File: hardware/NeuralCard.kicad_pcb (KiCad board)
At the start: 2 copper layers, 85.6 x 54 mm, 57 parts, among them J1 ProgPads, SW1 SW-SMD_4P-L5.1-W5.1-P3.70-LS6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, SW2 SW-SMD_4P-L5.1-W5.1-P3.70-LS6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, SW3 SW_SPDT_Shouhan_MSK12C02, U1 WIRELM-SMD_ESP32-S3-WROOM-1, U2 LGA-14_L3.0-W2.5-P0.50-TL, U4 SO-8_L4.9-W3.9-P1.27-LS5.9-BL

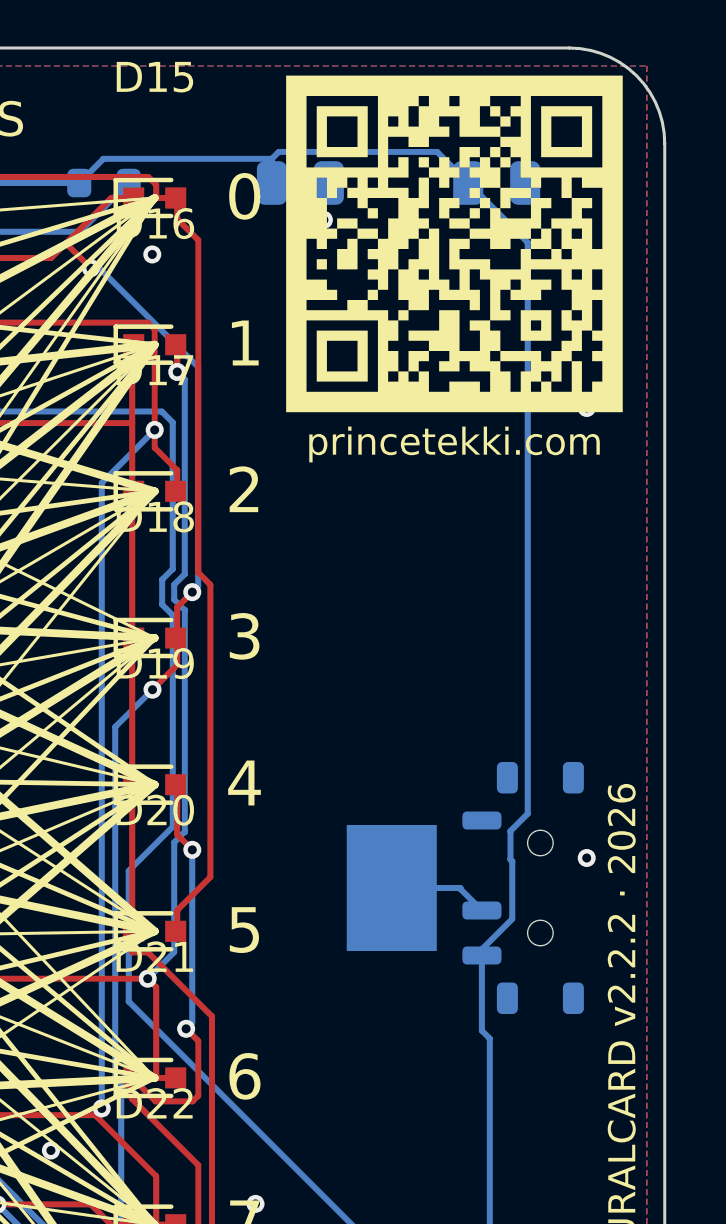
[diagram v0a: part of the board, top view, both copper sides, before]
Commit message: feat: place usb parts
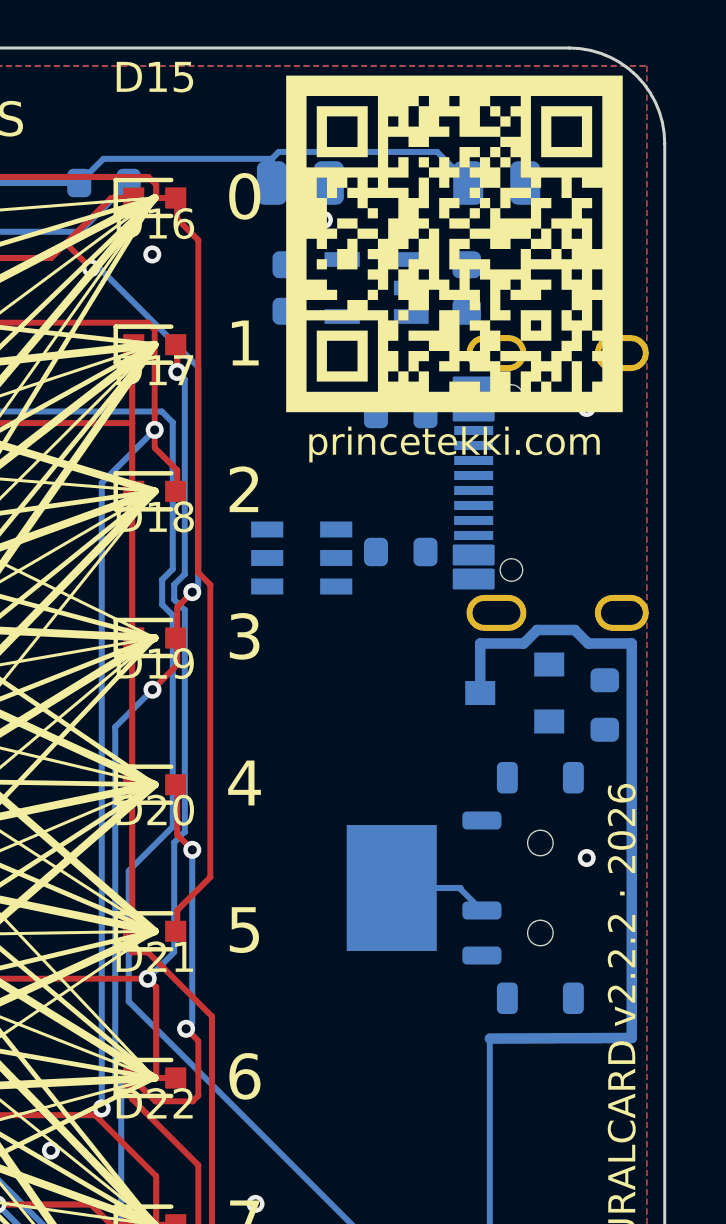
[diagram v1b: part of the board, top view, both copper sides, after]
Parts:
- added C6: 1uF, C_0603_1608Metric, B.Cu at (73.0, 8.00)
- added C7: 1uF, C_0603_1608Metric, B.Cu at (79.0, 8.00)
- added J2: TYPE-C-31-M-12, USB-C_SMD-TYPE-C-31-M-12_1, B.Cu at (81.7, 14.5)
- added Q1: AO3401A, SOT-23_L2.9-W1.3-P1.90-LS2.4-BR, B.Cu at (80.6, 21.5)
- added R13: 100k, R_0603_1608Metric, B.Cu at (83.6, 21.9)
- added R7: 5.1k, R_0603_1608Metric, B.Cu at (76.8, 12.2)
- added R8: 5.1k, R_0603_1608Metric, B.Cu at (76.8, 16.8)
- added U3: ME6211C33M5G-N, SOT-23-5_L3.0-W1.7-P0.95-LS2.8-BL, B.Cu at (76.0, 8.00)
- added U5: USBLC6-2SC6, SOT-23-6_L2.9-W1.6-P0.95-LS2.8-BL, B.Cu at (73.5, 17.0)
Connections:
- SW3 pad 3: +3V3 -> VBAT_SW
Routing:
- net +3V3: track 253.2 -> 248.0 mm

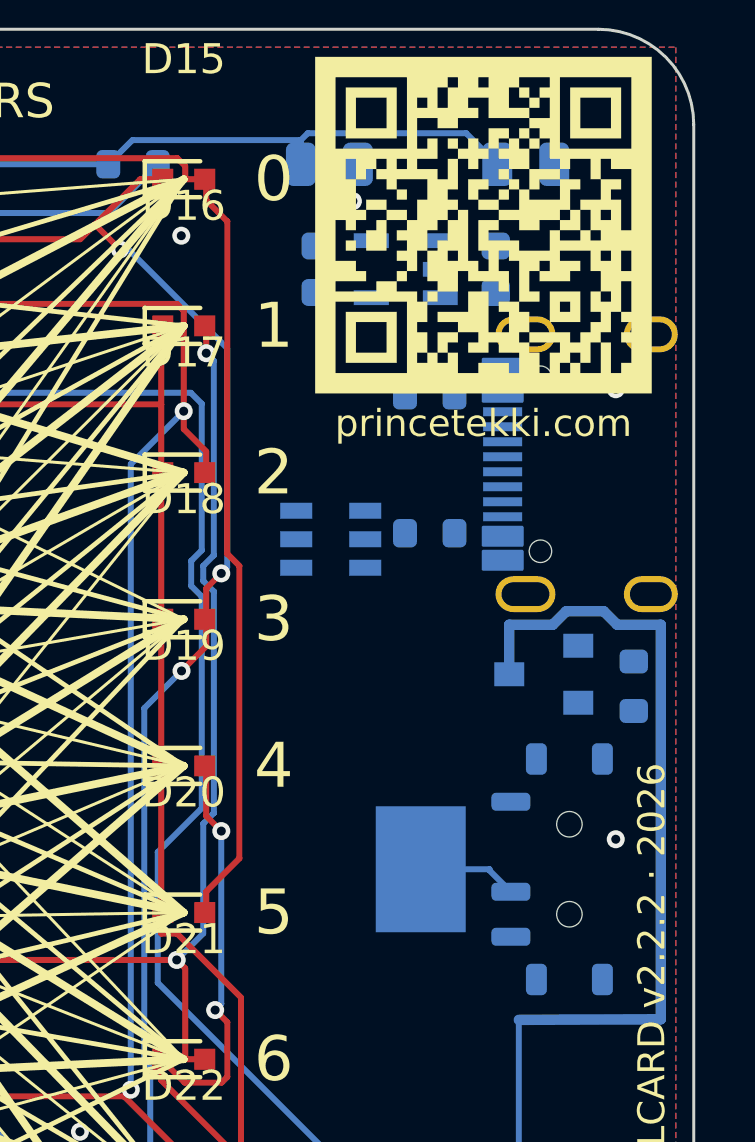
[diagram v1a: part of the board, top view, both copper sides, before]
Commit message: feat: route usb power
Power half of the USB section routed directly (skills verify, not design - per the
Kilikits locked decision the design work is done inline, geometry-queried, and the
skill review runs after).

Six DRC iterations on a copy before the board was touched. Wrong assumptions that
each cost one iteration and are worth recording: J2, SW3, U5 and U3 all carry
rotated pads whose printed w x h is transposed; a GND stitching via sat exactly on
the planned +3V3 corridor; the phase-1 +3V3 link forms a wall at y19.4-19.85 that
VBUS must cross on F.Cu; the VBAT feed trace crosses the only B.Cu channel to Q1's
source, hence a second F.Cu hop.

Result: 41 violations = 40 baseline + 1 accepted (J2 hybrid attr), 13 unconnected
= 3 pre-existing islands + 10 from the still-unrouted DP/DM pair. VBUS, +3V3,
VBAT_SW, CC1, CC2 all routed; U1 pins 13/14 assigned USB_DM/USB_DP.

DP/DM remains: interleaved USB-C pinout needs via crossings at the connector and
a 45mm matched pair to U1 - deliberately deferred rather than rushed.
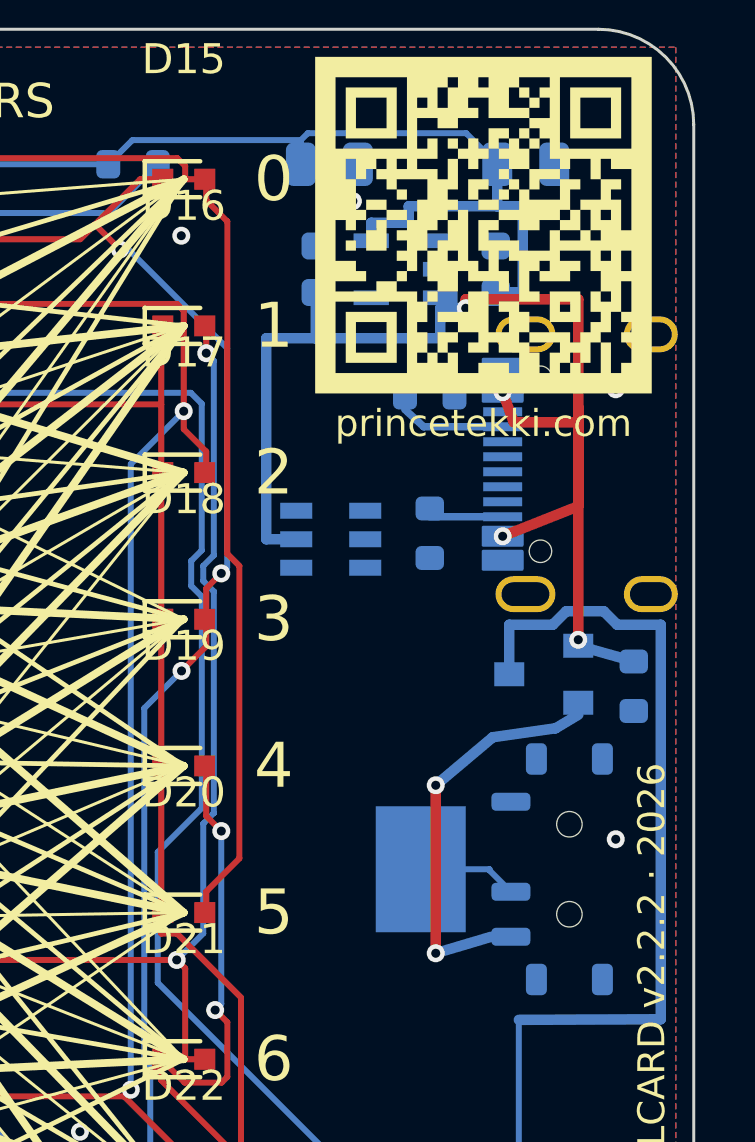
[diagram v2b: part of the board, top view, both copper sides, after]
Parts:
- turned R8 to -90 degrees
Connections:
- U1 pad 13: unconnected-(U1-IO19-Pad13) -> USB_DM
- U1 pad 14: unconnected-(U1-IO20-Pad14) -> USB_DP
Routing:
- net VBUS: track 0.00 -> 43.4 mm, vias 0 -> 4
- net VBAT_SW: track 0.00 -> 13.0 mm, vias 0 -> 2
- net +3V3: track 248.0 -> 258.7 mm
- net CC1: track 0.00 -> 3.48 mm
- net CC2: track 0.00 -> 2.43 mm

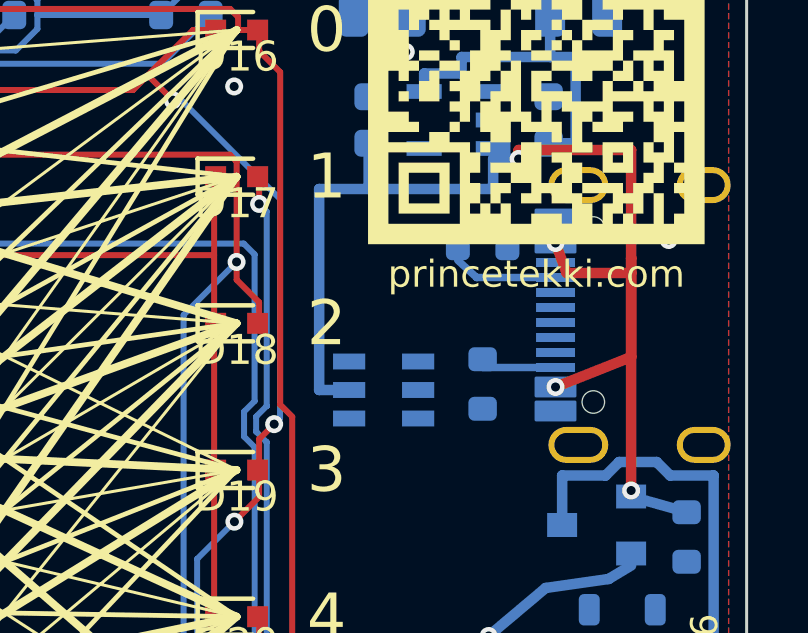
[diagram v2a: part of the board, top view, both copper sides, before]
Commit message: feat: route usb data phy
DP/DM routed J2 -> USBLC6 with the interleave resolved: USB-C presents DM-DP-DM-DP
at 0.5mm pitch, which no single layer can pair. DM ties its two pins in a compact
dogbone behind the pad column - usable because the connector's NPTHs sit 2mm away
in y - and DP's second pin hops on F.Cu into the main lane, the only place a via
fits once DM vacates the west stubs. Three earlier topologies each failed DRC on a
crossing; this one is planar by construction and DRC agrees: 41 violations, zero
USB-involved, identical to the accepted baseline.

VBUS's U5 feed moved to F.Cu with a via-in-pad so the west corridor is clear.

Remaining: the 48mm U5 -> U1 run. The obvious corridor is the charlieplex highway
and a first attempt collected 80+ violations - dropped on evidence, needs its own
corridor study.
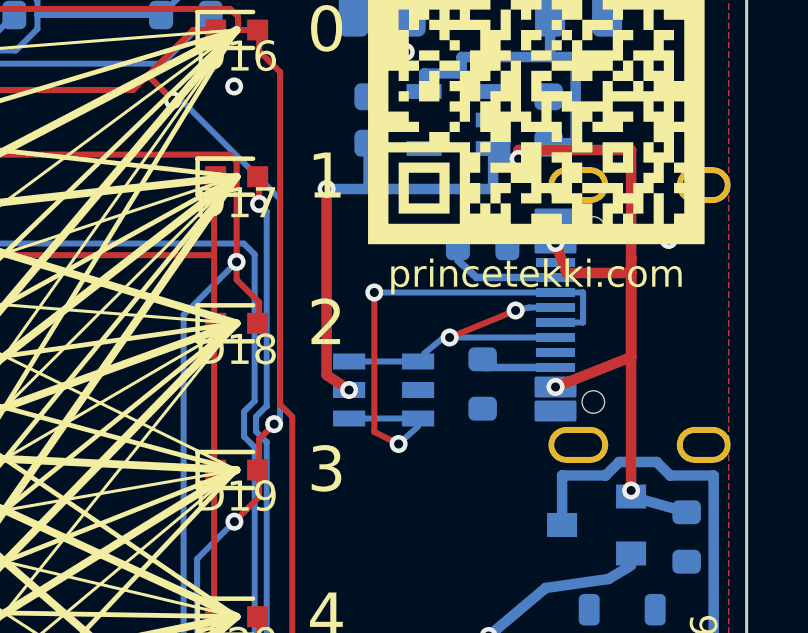
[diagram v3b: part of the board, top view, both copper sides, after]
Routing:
- net USB_DM: track 0.00 -> 14.6 mm, vias 0 -> 2
- net USB_DP: track 0.00 -> 8.22 mm, vias 0 -> 2
- net VBUS: track 43.4 -> 42.6 mm, vias 4 -> 6
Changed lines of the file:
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@@
 		(net "SDA")
 	)
+	(segment
+		(start 77.9 14.35)
+		(end 75.7 15.25)
+		(width 0.2)
+		(layer "F.Cu")
+		(net "USB_DP")
+	)
+	(via
+		(at 77.9 14.35)
+		(size 0.6)
+		(drill 0.3)
+		(layers "F.Cu" "B.Cu")
+		(net "USB_DP")
+	)
+	(via
+		(at 75.7 15.25)
+		(size 0.6)
+		(drill 0.3)
+		(layers "F.Cu" "B.Cu")
+		(net "USB_DP")
+	)
+	(segment
+		(start 78.58 14.25)
+		(end 78.35 14.25)
+		(width 0.2)
+		(layer "B.Cu")
+		(net "USB_DP")
+	)
+	(segment
+		(start 75.5 15.25)
+		(end 74.85 15.785)
+		(width 0.2)
+		(layer "B.Cu")
+		(net "USB_DP")
+	)
+	(segment
+		(start 78.58 15.25)
+		(end 75.5 15.25)
+		(width 0.2)
+		(layer "B.Cu")
+		(net "USB_DP")
+	)
+	(segment
+		(start 78.35 14.25)
+		(end 77.9 14.35)
+		(width 0.2)
+		(layer "B.Cu")
+		(net "USB_DP")
+	)
+	(segment
+		(start 74.115 16.05)
+		(end 72.885 16.05)
+		(width 0.2)
+		(layer "B.Cu")
+		(net "USB_DP")
+	)
 	(via
 		(at 10.806 5.734)
@@
 		(layers "F.Cu" "B.Cu")
 		(net "GND")
+	)
+	(segment
+		(start 73.19 13.75)
+		(end 73.19 18.4)
+		(width 0.2)
+		(layer "F.Cu")
+		(net "USB_DM")
+	)
+	(segment
+		(start 73.19 18.4)
+		(end 74 18.8)
+		(width 0.2)
+		(layer "F.Cu")
+		(net "USB_DM")
+	)
+	(via
+		(at 74 18.8)
+		(size 0.6)
+		(drill 0.3)
+		(layers "F.Cu" "B.Cu")
+		(net "USB_DM")
+	)
+	(via
+		(at 73.19 13.75)
+		(size 0.6)
+		(drill 0.3)
+		(layers "F.Cu" "B.Cu")
+		(net "USB_DM")
+	)
+	(segment
+		(start 74.115 17.95)
+		(end 72.885 17.95)
+		(width 0.2)
+		(layer "B.Cu")
+		(net "USB_DM")
+	)
+	(segment
+		(start 78.58 13.75)
+		(end 73.19 13.75)
+		(width 0.2)
+		(layer "B.Cu")
+		(net "USB_DM")
+	)
+	(segment
+		(start 74 18.8)
+		(end 74.65 18.215)
+		(width 0.2)
+		(layer "B.Cu")
+		(net "USB_DM")
+	)
+	(segment
+		(start 79.88 14.75)
+		(end 80.15 14.75)
+		(width 0.2)
+		(layer "B.Cu")
+		(net "USB_DM")
+	)
+	(segment
+		(start 80.15 13.75)
+		(end 79.88 13.75)
+		(width 0.2)
+		(layer "B.Cu")
+		(net "USB_DM")
+	)
+	(segment
+		(start 80.15 14.75)
+		(end 80.15 13.75)
+		(width 0.2)
+		(layer "B.Cu")
+		(net "USB_DM")
 	)
 	(segment
@@
 	)
 	(segment
+		(start 71.6 16.5)
+		(end 72.35 17)
+		(width 0.35)
+		(layer "F.Cu")
+		(net "VBUS")
+	)
+	(segment
 		(start 81.75 12.6)
 		(end 81.75 9)
@@
 		(net "VBUS")
 	)
+	(segment
+		(start 71.6 10.3)
+		(end 71.6 16.5)
+		(width 0.35)
+		(layer "F.Cu")
+		(net "VBUS")
+	)
 	(via
 		(at 79.23 12.1)
+		(size 0.6)
+		(drill 0.3)
+		(layers "F.Cu" "B.Cu")
+		(net "VBUS")
+	)
+	(via
+		(at 71.6 10.3)
+		(size 0.6)
+		(drill 0.3)
+		(layers "F.Cu" "B.Cu")
+		(net "VBUS")
+	)
+	(via
+		(at 72.35 17)
 		(size 0.6)
 		(drill 0.3)
@@
 	(segment
 		(start 73 10.3)
-		(end 71.35 10.3)
-		(width 0.35)
-		(layer "B.Cu")
-		(net "VBUS")
-	)
-	(segment
-		(start 71.35 17)
-		(end 72.35 17)
+		(end 71.6 10.3)
 		(width 0.35)
 		(layer "B.Cu")
@@
 		(width 0.35)
 		(layer "B.Cu")
-		(net "VBUS")
-	)
-	(segment
-		(start 71.35 10.3)
-		(end 71.35 17)
-		(width 0.35)
-		(layer "B.Cu")

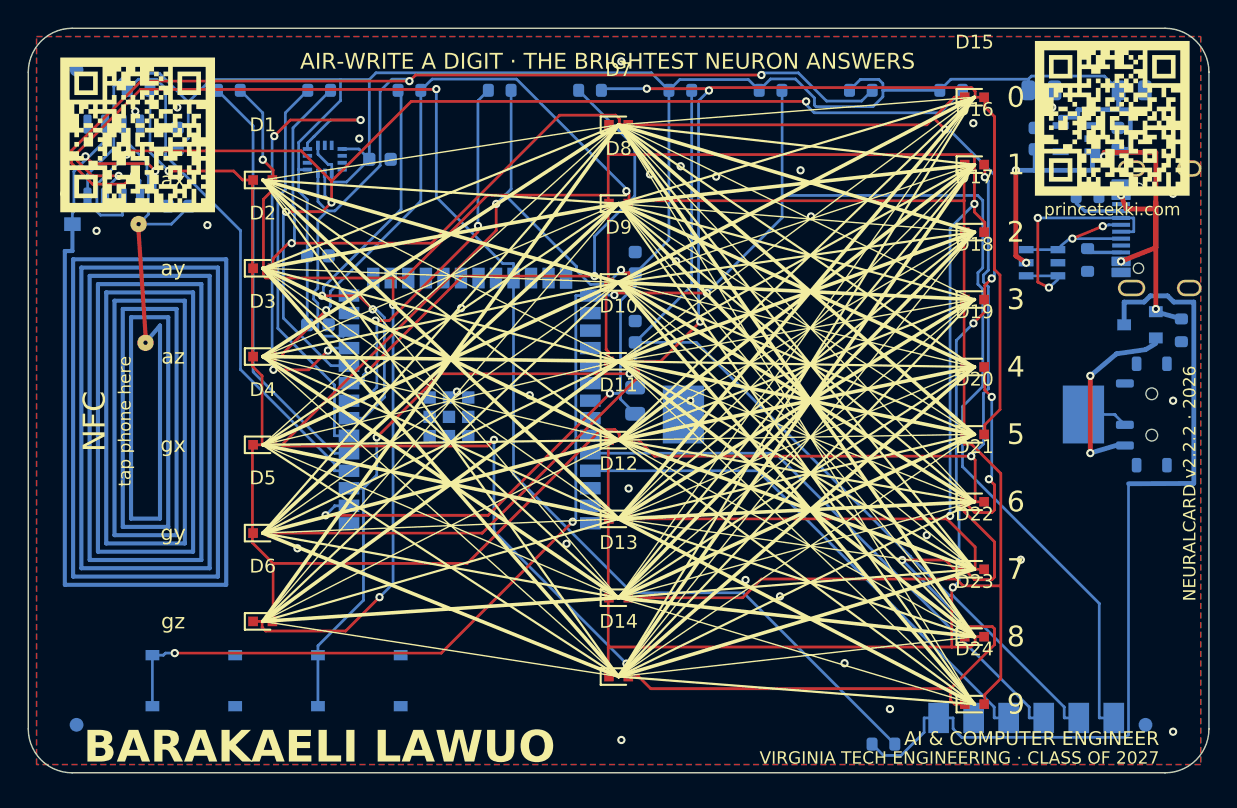
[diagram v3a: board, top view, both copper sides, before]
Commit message: route usb differential pair
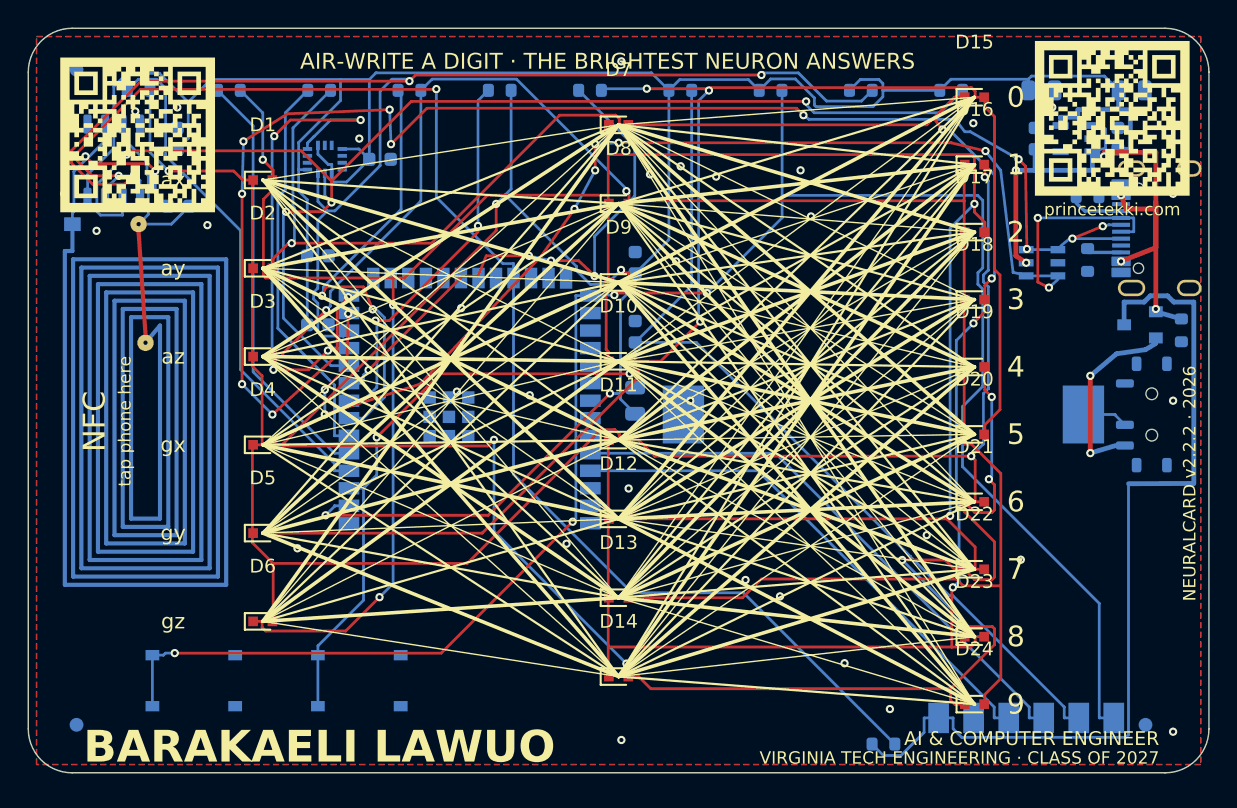
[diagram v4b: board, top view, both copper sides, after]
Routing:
- net USB_DP: track 8.22 -> 108.3 mm, vias 2 -> 12
- net USB_DM: track 14.6 -> 90.5 mm, vias 2 -> 10
- net VBUS: track 42.6 -> 45.8 mm
- net CHX6: track 37.7 -> 39.2 mm, vias 2 -> 4
- net CHX4: track 31.5 -> 32.6 mm
